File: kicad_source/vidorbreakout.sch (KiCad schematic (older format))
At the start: 12 parts, among them CN1 TE_2041119-2, CN2 CONN_01X18, CN3 CONN_01X18

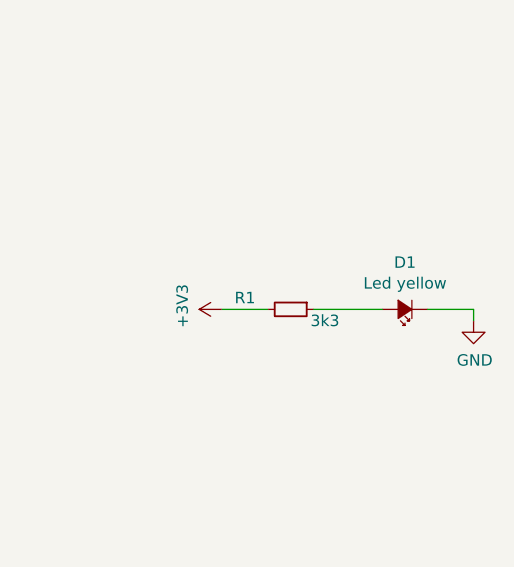
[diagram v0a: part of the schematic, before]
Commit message: reviewed  layout, added silkscreen, updated part values for aisler
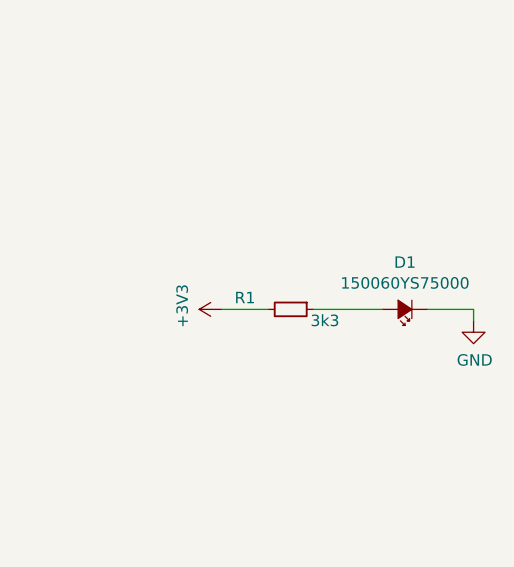
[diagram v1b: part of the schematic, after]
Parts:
- D1: value Led yellow -> 150060YS75000
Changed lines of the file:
@@
 P 10350 5900
 F 0 "D1" H 10350 5695 50  0000 C CNN
-F 1 "Led yellow" H 10350 5786 50  0000 C CNN
+F 1 "150060YS75000" H 10350 5786 50  0000 C CNN
 F 2 "LEDs:LED_0603" V 10350 5900 50  0001 C CNN
 F 3 "" V 10350 5900 50  0000 C CNN
